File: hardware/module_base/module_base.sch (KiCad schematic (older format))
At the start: 19 parts, among them J2 Conn_01x24_Female, J3 Conn_01x24_Female, J4 Conn_01x06_Male, Q1 Q_NMOS_GSD, Q2 Q_NMOS_GSD, Q3 Q_NMOS_GSD, Q4 Q_NMOS_GSD, Q5 Q_NMOS_GSD, Q6 Q_NMOS_GSD, U2 HT1632C-52LQFP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

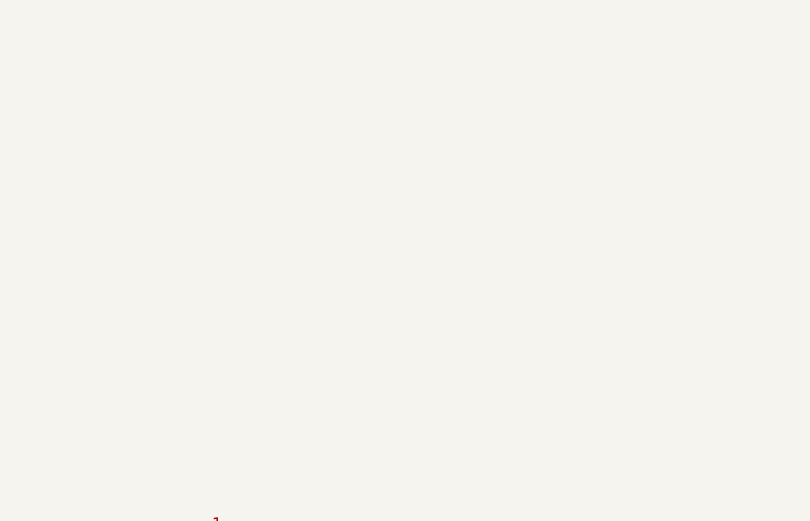
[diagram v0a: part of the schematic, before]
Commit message: Recreate timer module with single PCB, clean up libraries
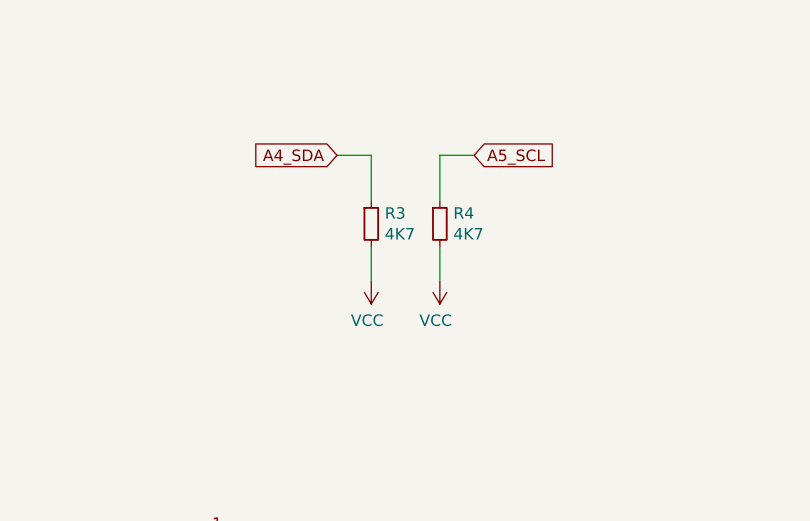
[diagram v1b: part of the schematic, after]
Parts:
- added R3, R4: 4K7, Resistor_SMD:R_0603_1608Metric_Pad1.05x0.95mm_HandSolder, symbol Device:R_Small
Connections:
- net A4_SDA: now also R3.1
- net A5_SCL: now also R4.1
- net VCC: now also R3.2, R4.2
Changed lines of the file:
@@
 	1    0    0    -1
 $EndComp
+$Comp
+L Device:R_Small R3
+U 1 1 5ECD8FF2
+P 7200 2600
+F 0 "R3" H 7259 2646 50  0000 L CNN
+F 1 "4K7" H 7259 2555 50  0000 L CNN
+F 2 "Resistor_SMD:R_0603_1608Metric_Pad1.05x0.95mm_HandSolder" H 7200 2600 50  0001 C CNN
+F 3 "~" H 7200 2600 50  0001 C CNN
+	1    7200 2600
+	1    0    0    -1
+$EndComp
+$Comp
+L Device:R_Small R4
+U 1 1 5ECD99DE
+P 7500 2600
+F 0 "R4" H 7559 2646 50  0000 L CNN
+F 1 "4K7" H 7559 2555 50  0000 L CNN
+F 2 "Resistor_SMD:R_0603_1608Metric_Pad1.05x0.95mm_HandSolder" H 7500 2600 50  0001 C CNN
+F 3 "~" H 7500 2600 50  0001 C CNN
+	1    7500 2600
+	1    0    0    -1
+$EndComp
+$Comp
+L power:VCC #PWR0113
+U 1 1 5ECD9D82
+P 7200 2850
+F 0 "#PWR0113" H 7200 2700 50  0001 C CNN
+F 1 "VCC" H 7218 3023 50  0000 C CNN
+F 2 "" H 7200 2850 50  0001 C CNN
+F 3 "" H 7200 2850 50  0001 C CNN
+	1    7200 2850
+	-1   0    0    1
+$EndComp
+$Comp
+L power:VCC #PWR0114
+U 1 1 5ECDA344
+P 7500 2850
+F 0 "#PWR0114" H 7500 2700 50  0001 C CNN
+F 1 "VCC" H 7518 3023 50  0000 C CNN
+F 2 "" H 7500 2850 50  0001 C CNN
+F 3 "" H 7500 2850 50  0001 C CNN
+	1    7500 2850
+	-1   0    0    1
+$EndComp
+Wire Wire Line
+	7500 2850 7500 2700
+Wire Wire Line
+	7200 2700 7200 2850
+Text GLabel 7050 2300 0    50   Input ~ 0
+A4_SDA
+Text GLabel 7650 2300 2    50   Input ~ 0
+A5_SCL
+Wire Wire Line
+	7050 2300 7200 2300
+Wire Wire Line
+	7200 2300 7200 2500
+Wire Wire Line
+	7500 2500 7500 2300
+Wire Wire Line
+	7500 2300 7650 2300
 $EndSCHEMATC

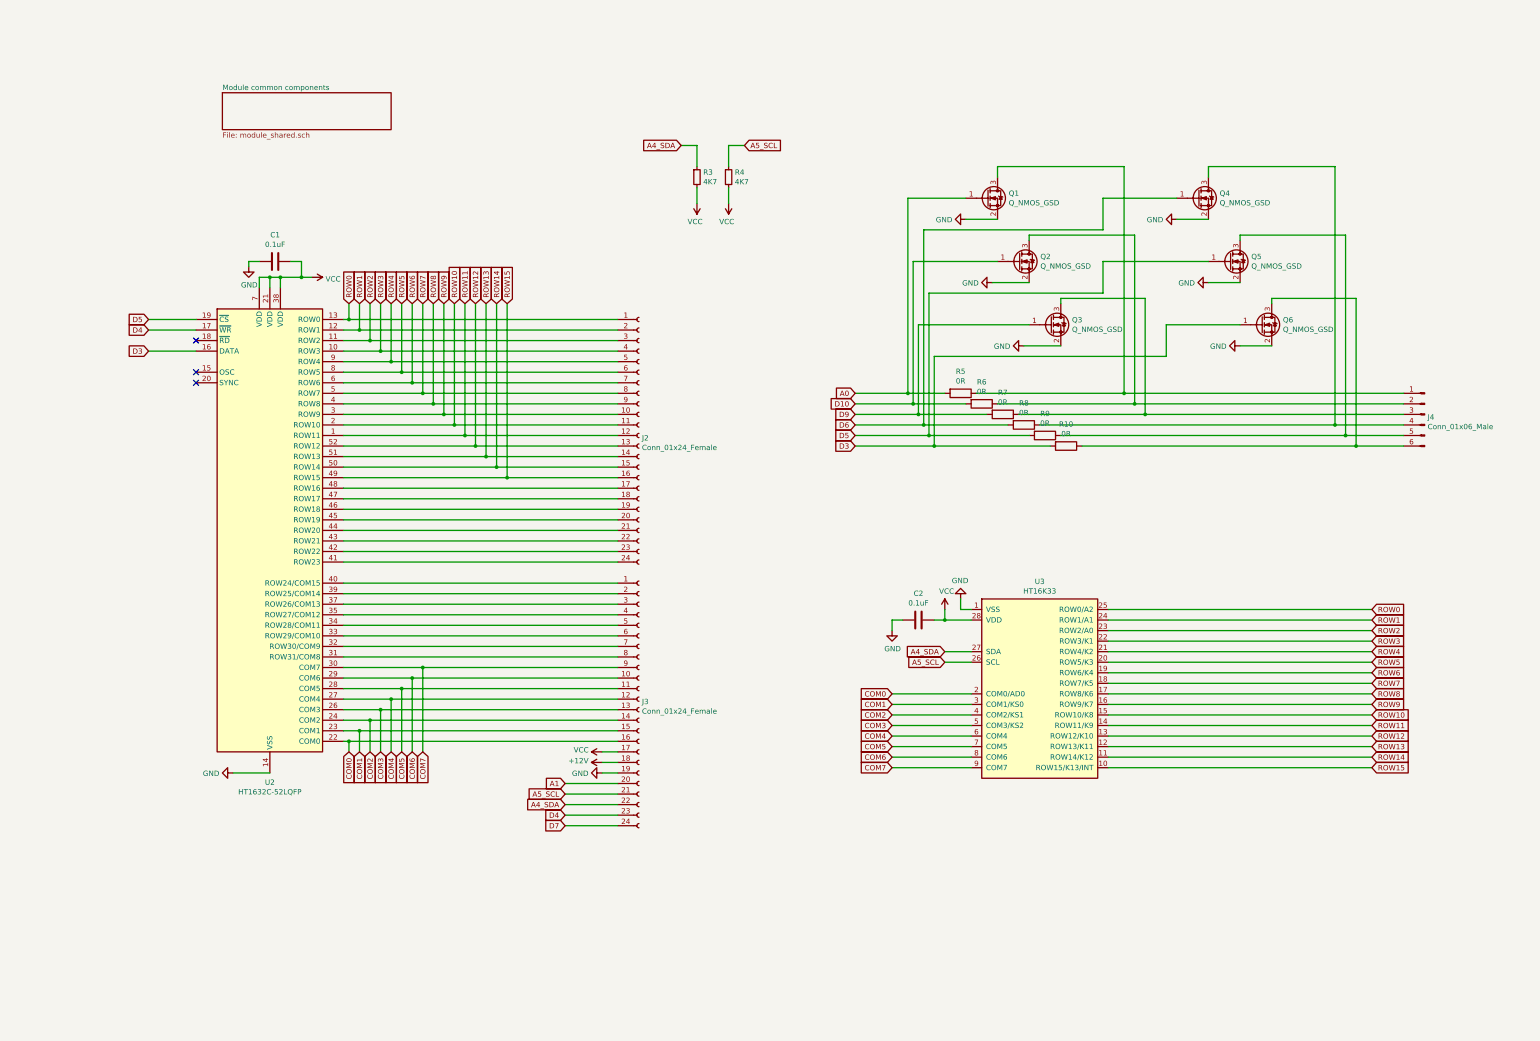
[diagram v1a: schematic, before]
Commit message: Redo prototyping module layout: CAN module on back, two rows of pins
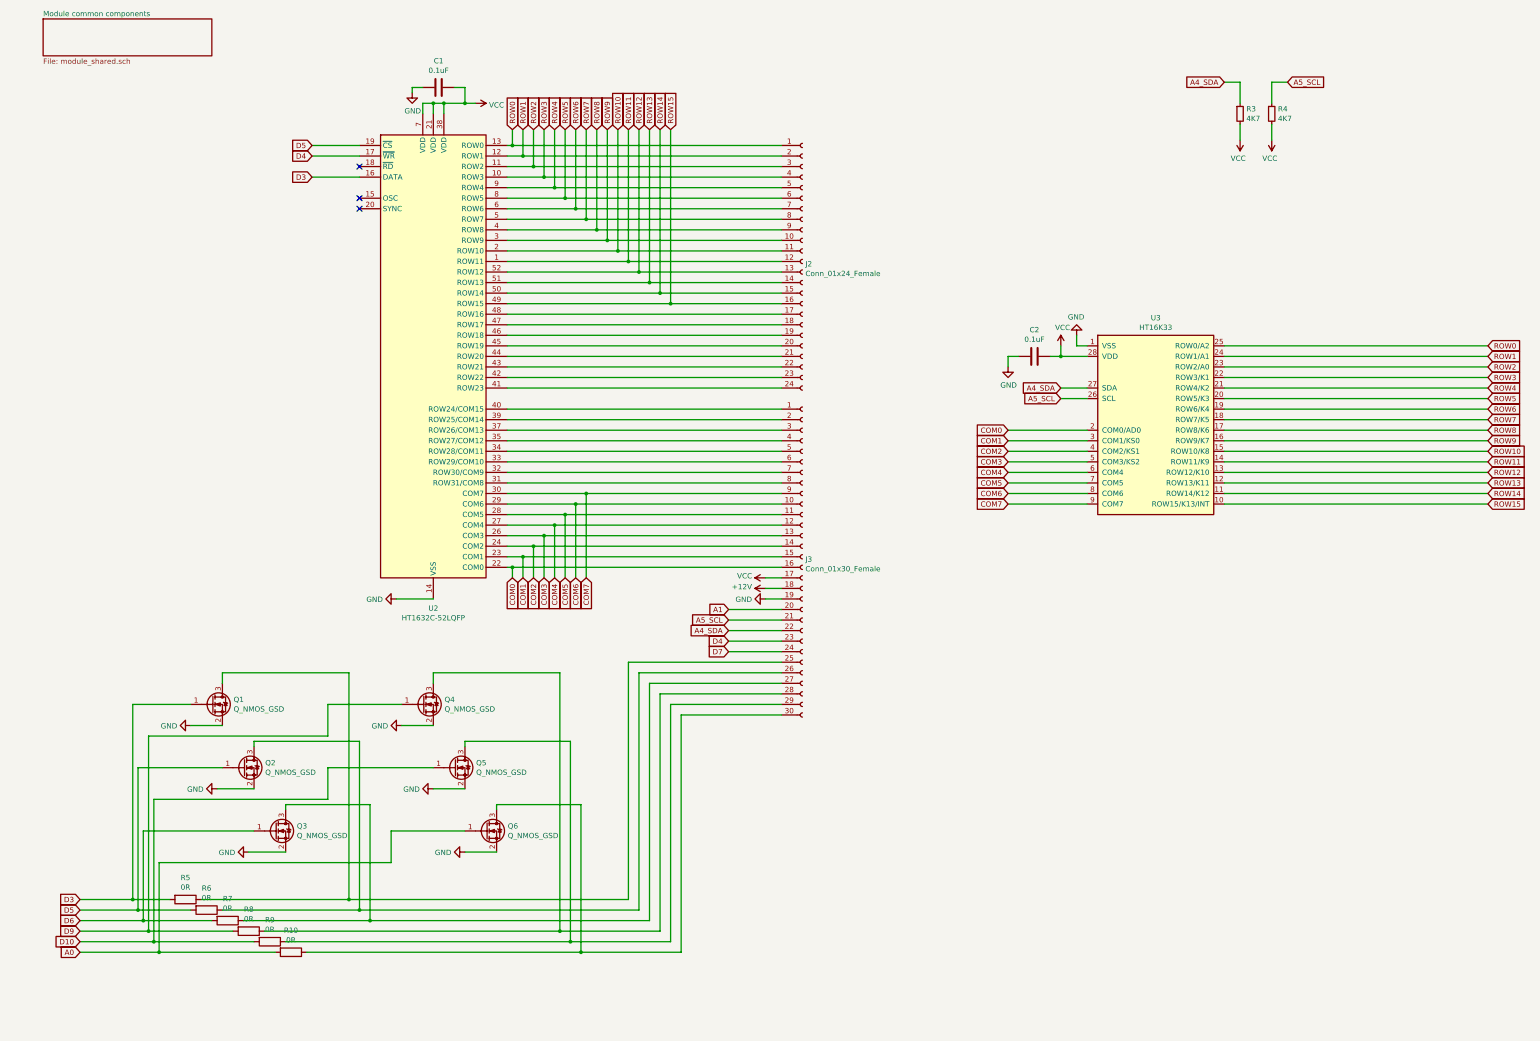
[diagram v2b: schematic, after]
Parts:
- removed J3: Conn_01x24_Female, Connector_PinHeader_2.54mm:PinHeader_1x24_P2.54mm_Vertical, symbol Connector:Conn_01x24_Female
- removed J4: Conn_01x06_Male, Connector_PinHeader_2.54mm:PinHeader_1x06_P2.54mm_Vertical, symbol Connector:Conn_01x06_Male
- added J3: Conn_01x30_Female, Connector_PinSocket_2.54mm:PinSocket_1x30_P2.54mm_Vertical, symbol Connector:Conn_01x30_Female
- J2: footprint Connector_PinHeader_2.54mm:PinHeader_1x24_P2.54mm_Vertical -> Connector_PinSocket_2.54mm:PinSocket_1x24_P2.54mm_Vertical
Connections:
- net +12V: now also J3.18 (Pin_18)
- net A0: now also Q6.1 (G), R10.2; no longer Q1.1 (G), R5.2
- net A1: now also J3.20 (Pin_20)
- net A4_SDA: now also J3.22 (Pin_22)
- net A5_SCL: now also J3.21 (Pin_21)
- net COM0: now also J3.16 (Pin_16)
- net COM1: now also J3.15 (Pin_15)
- net COM2: now also J3.14 (Pin_14)
- net COM3: now also J3.13 (Pin_13)
- net COM4: now also J3.12 (Pin_12)
- net COM5: now also J3.11 (Pin_11)
- net COM6: now also J3.10 (Pin_10)
- net COM7: now also J3.9 (Pin_9)
- net D10: now also Q5.1 (G), R9.2; no longer Q2.1 (G), R6.2
- net D3: now also Q1.1 (G), R5.2; no longer Q6.1 (G), R10.2
- net D4: now also J3.23 (Pin_23)
- net D5: now also Q2.1 (G), R6.2; no longer Q5.1 (G), R9.2
- net D6: now also Q3.1 (G), R7.2; no longer Q4.1 (G), R8.2
- net D7: now also J3.24 (Pin_24)
- net D9: now also Q4.1 (G), R8.2; no longer Q3.1 (G), R7.2
- net GND: now also J3.19 (Pin_19)
- net VCC: now also J3.17 (Pin_17)
- net at U2.31 (ROW31/COM8): now also J3.8 (Pin_8)
- net at U2.32 (ROW30/COM9): now also J3.7 (Pin_7)
- net at U2.33 (ROW29/COM10): now also J3.6 (Pin_6)
- net at U2.34 (ROW28/COM11): now also J3.5 (Pin_5)
- net at U2.35 (ROW27/COM12): now also J3.4 (Pin_4)
- net at U2.37 (ROW26/COM13): now also J3.3 (Pin_3)
- net at U2.39 (ROW25/COM14): now also J3.2 (Pin_2)
- net at U2.40 (ROW24/COM15): now also J3.1 (Pin_1)
- net at Q1.3 (D), R5.1: now also J3.25 (Pin_25)
- net at Q2.3 (D), R6.1: now also J3.26 (Pin_26)
- net at Q3.3 (D), R7.1: now also J3.27 (Pin_27)
- net at Q4.3 (D), R8.1: now also J3.28 (Pin_28)
- net at Q5.3 (D), R9.1: now also J3.29 (Pin_29)
- net at Q6.3 (D), R10.1: now also J3.30 (Pin_30)
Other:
- moved on the sheet: C1, C2, J2, Q1, Q2, Q3, Q4, Q5, Q6, R10, R3, R4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

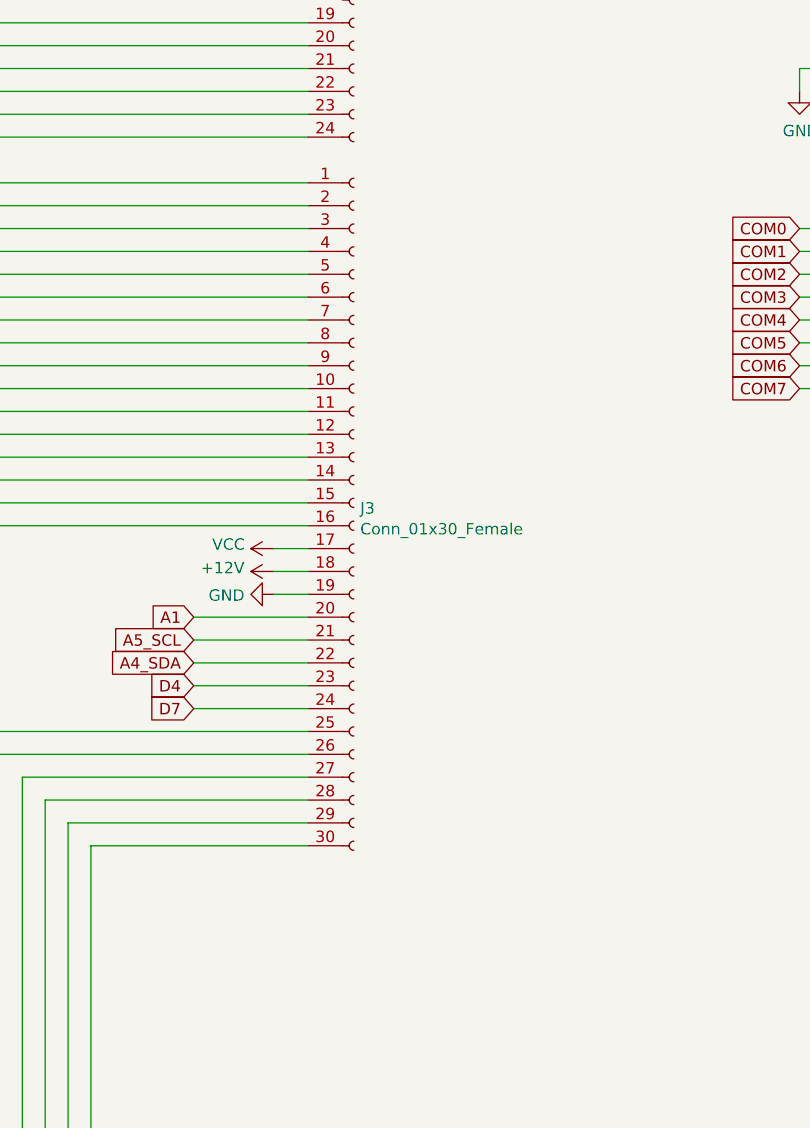
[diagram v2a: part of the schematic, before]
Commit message: ModuleBase PCB: add lots of mounting holes and some grounds
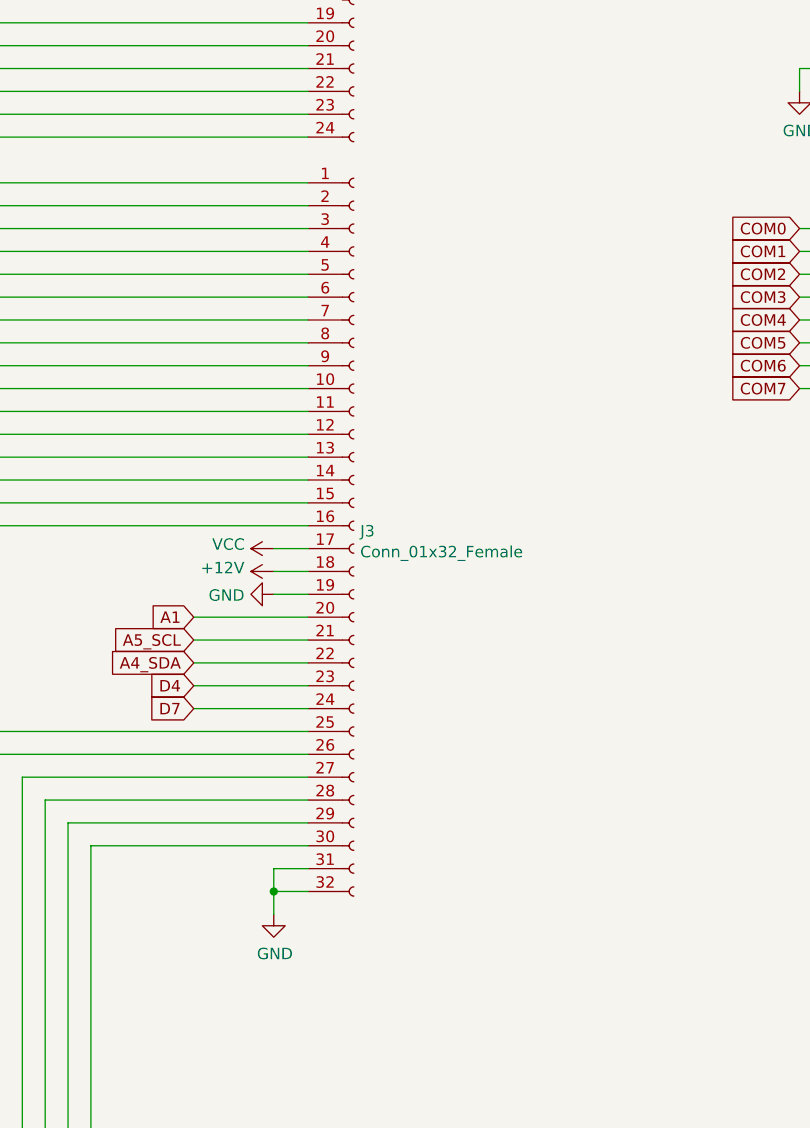
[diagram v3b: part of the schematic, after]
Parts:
- removed J3: Conn_01x30_Female, Connector_PinSocket_2.54mm:PinSocket_1x30_P2.54mm_Vertical, symbol Connector:Conn_01x30_Female
- added J3: Conn_01x32_Female, Connector_PinSocket_2.54mm:PinSocket_1x32_P2.54mm_Vertical, symbol Connector:Conn_01x32_Female
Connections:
- net +12V: now also J3.18 (Pin_18)
- net A1: now also J3.20 (Pin_20)
- net A4_SDA: now also J3.22 (Pin_22)
- net A5_SCL: now also J3.21 (Pin_21)
- net COM0: now also J3.16 (Pin_16)
- net COM1: now also J3.15 (Pin_15)
- net COM2: now also J3.14 (Pin_14)
- net COM3: now also J3.13 (Pin_13)
- net COM4: now also J3.12 (Pin_12)
- net COM5: now also J3.11 (Pin_11)
- net COM6: now also J3.10 (Pin_10)
- net COM7: now also J3.9 (Pin_9)
- net D4: now also J3.23 (Pin_23)
- net D7: now also J3.24 (Pin_24)
- net GND: now also J3.19 (Pin_19), J3.31 (Pin_31), J3.32 (Pin_32)
- net VCC: now also J3.17 (Pin_17)
- net at U2.31 (ROW31/COM8): now also J3.8 (Pin_8)
- net at U2.32 (ROW30/COM9): now also J3.7 (Pin_7)
- net at U2.33 (ROW29/COM10): now also J3.6 (Pin_6)
- net at U2.34 (ROW28/COM11): now also J3.5 (Pin_5)
- net at U2.35 (ROW27/COM12): now also J3.4 (Pin_4)
- net at U2.37 (ROW26/COM13): now also J3.3 (Pin_3)
- net at U2.39 (ROW25/COM14): now also J3.2 (Pin_2)
- net at U2.40 (ROW24/COM15): now also J3.1 (Pin_1)
- net at Q1.3 (D), R5.1: now also J3.25 (Pin_25)
- net at Q2.3 (D), R6.1: now also J3.26 (Pin_26)
- net at Q3.3 (D), R7.1: now also J3.27 (Pin_27)
- net at Q4.3 (D), R8.1: now also J3.28 (Pin_28)
- net at Q5.3 (D), R9.1: now also J3.29 (Pin_29)
- net at Q6.3 (D), R10.1: now also J3.30 (Pin_30)
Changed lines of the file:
@@
 Wire Wire Line
 	12650 1700 12800 1700
-$Comp
-L Connector:Conn_01x30_Female J3
-U 1 1 5ED95C02
-P 8200 6200
-F 0 "J3" H 8228 6176 50  0000 L CNN
-F 1 "Conn_01x30_Female" H 8228 6085 50  0000 L CNN
-F 2 "Connector_PinSocket_2.54mm:PinSocket_1x30_P2.54mm_Vertical" H 8200 6200 50  0001 C CNN
-F 3 "~" H 8200 6200 50  0001 C CNN
-	1    8200 6200
-	1    0    0    -1
-$EndComp
 Wire Wire Line
 	6550 9450 6550 7200
@@
 Wire Wire Line
 	6100 9950 7050 9950
+$Comp
+L Connector:Conn_01x32_Female J3
+U 1 1 6097D987
+P 8200 6300
+F 0 "J3" H 8228 6276 50  0000 L CNN
+F 1 "Conn_01x32_Female" H 8228 6185 50  0000 L CNN
+F 2 "Connector_PinSocket_2.54mm:PinSocket_1x32_P2.54mm_Vertical" H 8200 6300 50  0001 C CNN
+F 3 "~" H 8200 6300 50  0001 C CNN
+	1    8200 6300
+	1    0    0    -1
+$EndComp
+$Comp
+L power:GND #PWR?
+U 1 1 6098995E
+P 7850 8000
+F 0 "#PWR?" H 7850 7750 50  0001 C CNN
+F 1 "GND" H 7855 7827 50  0000 C CNN
+F 2 "" H 7850 8000 50  0001 C CNN
+F 3 "" H 7850 8000 50  0001 C CNN
+	1    7850 8000
+	1    0    0    -1
+$EndComp
+Wire Wire Line
+	7850 8000 7850 7900
+Wire Wire Line
+	7850 7800 8000 7800
+Wire Wire Line
+	8000 7900 7850 7900
+Connection ~ 7850 7900
+Wire Wire Line
+	7850 7900 7850 7800
 $EndSCHEMATC

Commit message: ModuleBase PCB: expose Arduino pins + SPI + more GND/5V
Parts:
- added J4, J5: Conn_01x15_Female, Connector_PinSocket_2.54mm:PinSocket_1x15_P2.54mm_Vertical, symbol Connector:Conn_01x15_Female
- C1, C2: footprint Capacitor_SMD:C_0603_1608Metric_Pad1.05x0.95mm_HandSolder -> Capacitor_SMD:C_0603_1608Metric_Pad1.08x0.95mm_HandSolder
- J3: value Conn_01x32_Female -> Conn_01x36_Female; footprint Connector_PinSocket_2.54mm:PinSocket_1x32_P2.54mm_Vertical -> Connector_PinSocket_2.54mm:PinSocket_1x36_P2.54mm_Vertical; symbol Connector:Conn_01x32_Female -> Connector:Conn_01x36_Female
- Q1, Q2, Q3, Q4, Q5, Q6: footprint Package_TO_SOT_SMD:SOT-23 -> Package_TO_SOT_SMD:SOT-23_Handsoldering
- R10, R3, R4, R5, R6, R7, R8, R9: footprint Resistor_SMD:R_0603_1608Metric_Pad1.05x0.95mm_HandSolder -> Resistor_SMD:R_0603_1608Metric_Pad0.98x0.95mm_HandSolder
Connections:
- net +12V: now also J3.19 (Pin_19); no longer J3.18 (Pin_18)
- net A0: now also J4.4 (Pin_4); no longer R10.2
- net A1: now also J4.5 (Pin_5); no longer J3.20 (Pin_20)
- net A4_SDA: now also J3.21 (Pin_21), J4.8 (Pin_8); no longer J3.22 (Pin_22)
- net A5_SCL: now also J3.20 (Pin_20), J4.9 (Pin_9); no longer J3.21 (Pin_21)
- net D10: now also J5.3 (Pin_3); no longer R9.2
- net D3: now also J5.10 (Pin_10); no longer R5.2
- net D4: now also J5.9 (Pin_9); no longer J3.23 (Pin_23)
- net D5: now also J5.8 (Pin_8); no longer R6.2
- net D6: now also J5.7 (Pin_7); no longer R7.2
- net D7: now also J5.6 (Pin_6); no longer J3.24 (Pin_24)
- net D9: now also J5.4 (Pin_4); no longer R8.2
- net GND: now also J3.33 (Pin_33), J3.34 (Pin_34), J3.35 (Pin_35), J3.36 (Pin_36), J4.14 (Pin_14), J5.12 (Pin_12); no longer J3.19 (Pin_19)
- net VCC: now also J3.18 (Pin_18), J4.12 (Pin_12)
- net at J3.25 (Pin_25), R5.1: no longer Q1.3 (D)
- net at J3.26 (Pin_26), R6.1: no longer Q2.3 (D)
- net at J3.27 (Pin_27), R7.1: no longer Q3.3 (D)
- net at J3.28 (Pin_28), R8.1: no longer Q4.3 (D)
- net at J3.29 (Pin_29), R9.1: no longer Q5.3 (D)
- net at J3.30 (Pin_30), R10.1: no longer Q6.3 (D)
- new net: Q1.3 (D), R5.2
- new net: Q2.3 (D), R6.2
- new net: Q3.3 (D), R7.2
- new net: Q4.3 (D), R8.2
- new net: Q5.3 (D), R9.2
- new net: Q6.3 (D), R10.2
- new net +3V3: J4.2 (Pin_2)
- new net A2_MODULE_READY: J4.6 (Pin_6)
- new net A3_MODULE_ENABLE: J4.7 (Pin_7)
- new net A6: J4.10 (Pin_10)
- new net A7: J4.11 (Pin_11)
- new net AREF: J4.3 (Pin_3)
- new net D0_RX: J5.14 (Pin_14)
- new net D11_MOSI: J3.24 (Pin_24), J5.2 (Pin_2)
- new net D12_MISO: J3.23 (Pin_23), J5.1 (Pin_1)
- new net D13_SCK: J3.22 (Pin_22), J4.1 (Pin_1)
- new net D1_TX: J5.15 (Pin_15)
- new net D2_CAN_INT: J5.11 (Pin_11)
- new net D8_CAN_CS: J5.5 (Pin_5)
- new net RST: J4.13 (Pin_13), J5.13 (Pin_13)
- new net VIN: J4.15 (Pin_15)
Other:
- moved on the sheet: Q1, Q2, Q3, Q4, Q5, Q6, R10, R5, R6, R7, R8, R9

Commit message: ModuleBase PCB: longer pads for HT1632C footprint
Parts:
- U2: footprint Package_QFP:LQFP-52_14x14mm_P1mm -> ProjectChips:QFP-52_14x14_Pitch1mm_HandSoldering
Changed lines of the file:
@@
 F 0 "U2" H 4700 1911 50  0000 C CNN
 F 1 "HT1632C-52LQFP" H 4700 1820 50  0000 C CNN
-F 2 "Package_QFP:LQFP-52_14x14mm_P1mm" V 4500 4350 50  0001 C CNN
+F 2 "ProjectChips:QFP-52_14x14_Pitch1mm_HandSoldering" V 4500 4350 50  0001 C CNN
 F 3 "http://www.holtek.com/documents/10179/116711/HT1632Cv170.pdf" V 4500 4350 50  0001 C CNN
 	1    4700 4300
